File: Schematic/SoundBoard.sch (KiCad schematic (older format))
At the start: 47 parts, among them J1 USB_B_Micro, J2 Conn_ARM_JTAG_SWD_10, SW1 SW_Push, SW2 SW_Push, U1 AMS1117-3.3, U2 STM32F405RGTx, U3 MCP4021-xxxxSN, U4 LM4562, U5 W25Q128JVS, Y1 25Mhz

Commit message: Perform layout
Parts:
- added C19, C21: 100n, Capacitor_SMD:C_0402_1005Metric, symbol Device:C
- added C20: 10u, Capacitor_SMD:C_0603_1608Metric, symbol Device:C
- C10, C11, C12, C13, C14, C15, C16, C17, C18, C2, C3, C8, C9: footprint Capacitor_SMD:C_0603_1608Metric -> Capacitor_SMD:C_0402_1005Metric
- FB1, FB2: footprint Inductor_SMD:L_0603_1608Metric -> Inductor_SMD:L_0805_2012Metric
- R5: footprint Resistor_SMD:R_0603_1608Metric -> Resistor_SMD:R_0402_1005Metric
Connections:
- net +3V3: now also C19.1, C20.1
- net GND: now also C19.2, C20.2, C21.2; no longer J1.6 (Shield)
- net NRESET: now also C21.1
- net USB_DM renamed USBD_N
- net USB_DP renamed USBD_P
- no-connect marks 39 -> 40
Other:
- moved on the sheet: D2, J1, R1

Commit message: Create BOM remove unnecessary files
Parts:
- C18: footprint Capacitor_SMD:C_0402_1005Metric -> Capacitor_SMD:C_0805_2012Metric
- D1: footprint Diode_SMD:D_0603_1608Metric -> Diode_SMD:D_SOD-123
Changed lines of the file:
@@
 F 0 "D1" H 1500 1234 50  0000 C CNN
 F 1 "D_Schottky" H 1500 1325 50  0000 C CNN
-F 2 "Diode_SMD:D_0603_1608Metric" H 1500 1450 50  0001 C CNN
+F 2 "Diode_SMD:D_SOD-123" H 1500 1450 50  0001 C CNN
 F 3 "~" H 1500 1450 50  0001 C CNN
 	1    1500 1450
@@
 F 0 "C18" V 8898 4750 50  0000 C CNN
 F 1 "10p" V 8989 4750 50  0000 C CNN
-F 2 "Capacitor_SMD:C_0402_1005Metric" H 9188 4600 50  0001 C CNN
+F 2 "Capacitor_SMD:C_0805_2012Metric" H 9188 4600 50  0001 C CNN
 F 3 "~" H 9150 4750 50  0001 C CNN
 	1    9150 4750

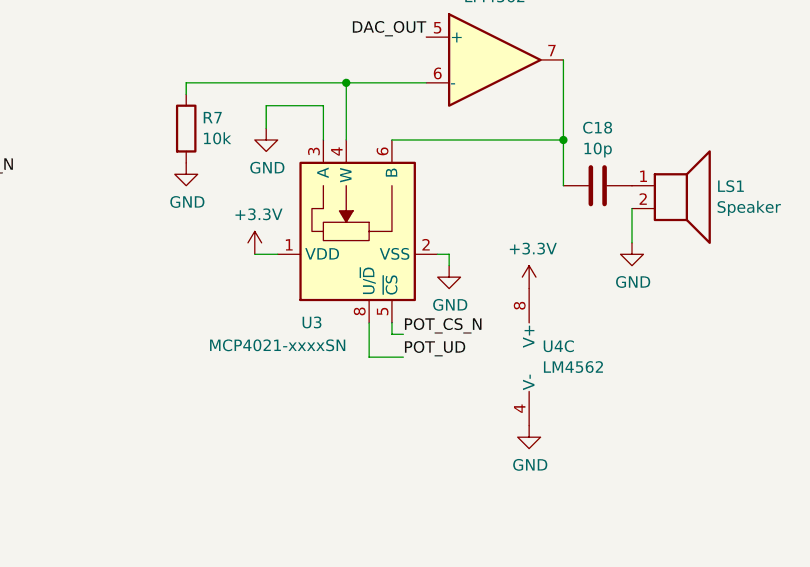
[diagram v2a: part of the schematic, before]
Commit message: Received rev 1 boards and performed initial testing
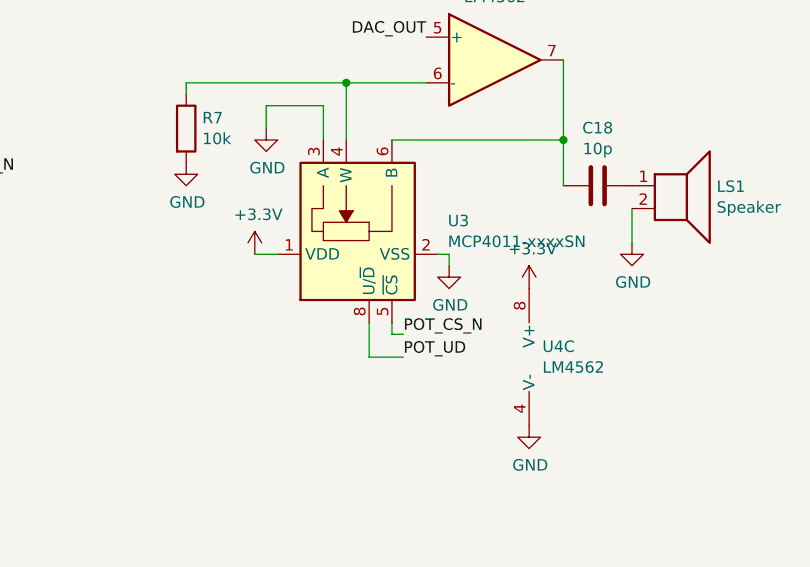
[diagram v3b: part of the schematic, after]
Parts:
- removed U3: MCP4021-xxxxSN, Package_SO:SOIC-8_3.9x4.9mm_P1.27mm, symbol Potentiometer_Digital:MCP4021-xxxxSN
- added U3: MCP4011-xxxxSN, Package_SO:SOIC-8_3.9x4.9mm_P1.27mm, symbol Potentiometer_Digital:MCP4011-xxxxSN
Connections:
- net +3V3: now also U3.1 (VDD)
- net GND: now also U3.2 (VSS), U3.3 (A)
- net POT_CS_N: now also U3.5 (~CS)
- net POT_UD: now also U3.8 (U/~D)
- net at C18.2, U4.7: now also U3.6 (B)
- net at R7.1, U4.6 (-): now also U3.4 (W)
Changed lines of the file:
@@
 Text Label 6250 4700 0    50   ~ 0
 POT_CS_N
-$Comp
-L Potentiometer_Digital:MCP4021-xxxxSN U3
-U 1 1 5EF33020
-P 8150 4950
-F 0 "U3" V 7750 5200 50  0000 C CNN
-F 1 "MCP4021-xxxxSN" V 7650 5350 50  0000 C CNN
-F 2 "Package_SO:SOIC-8_3.9x4.9mm_P1.27mm" H 8200 4700 50  0001 L CNN
-F 3 "http://ww1.microchip.com/downloads/en/DeviceDoc/21945e.pdf" H 8200 4400 50  0001 L CNN
-	1    8150 4950
-	0    -1   -1   0
-$EndComp
 Text Label 8300 5400 0    50   ~ 0
 POT_CS_N
@@
 	3200 5650 3400 5650
 NoConn ~ 950  6350
+$Comp
+L Potentiometer_Digital:MCP4011-xxxxSN U3
+U 1 1 5ED6F448
+P 8150 4950
+F 0 "U3" V 8196 4606 50  0000 R CNN
+F 1 "MCP4011-xxxxSN" V 8105 4606 50  0000 R CNN
+F 2 "Package_SO:SOIC-8_3.9x4.9mm_P1.27mm" H 8200 4700 50  0001 L CNN
+F 3 "http://ww1.microchip.com/downloads/en/DeviceDoc/21978c.pdf, SOIC-8" H 8200 4400 50  0001 L CNN
+	1    8150 4950
+	0    -1   -1   0
+$EndComp
 $EndSCHEMATC

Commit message: Rev 1 manufacturing update
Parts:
- removed U3: MCP4011-xxxxSN, Package_SO:SOIC-8_3.9x4.9mm_P1.27mm, symbol Potentiometer_Digital:MCP4011-xxxxSN
- added U3: MCP4021-xxxxSN, Package_SO:SOIC-8_3.9x4.9mm_P1.27mm, symbol Potentiometer_Digital:MCP4021-xxxxSN
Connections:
- net +3V3: now also U3.1 (VDD)
- net GND: now also U3.2 (VSS), U3.3 (A)
- net POT_CS_N: now also U3.5 (~CS)
- net POT_UD: now also U3.8 (U/~D)
- net at C18.2, U4.7: now also U3.6 (B)
- net at R7.1, U4.6 (-): now also U3.4 (W)
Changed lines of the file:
@@
 NoConn ~ 950  6350
 $Comp
-L Potentiometer_Digital:MCP4011-xxxxSN U3
-U 1 1 5ED6F448
+L Potentiometer_Digital:MCP4021-xxxxSN U3
+U 1 1 5EEB82C1
 P 8150 4950
 F 0 "U3" V 8196 4606 50  0000 R CNN
-F 1 "MCP4011-xxxxSN" V 8105 4606 50  0000 R CNN
+F 1 "MCP4021-xxxxSN" V 8105 4606 50  0000 R CNN
 F 2 "Package_SO:SOIC-8_3.9x4.9mm_P1.27mm" H 8200 4700 50  0001 L CNN
-F 3 "http://ww1.microchip.com/downloads/en/DeviceDoc/21978c.pdf, SOIC-8" H 8200 4400 50  0001 L CNN
+F 3 "http://ww1.microchip.com/downloads/en/DeviceDoc/21945e.pdf" H 8200 4400 50  0001 L CNN
 	1    8150 4950
 	0    -1   -1   0
